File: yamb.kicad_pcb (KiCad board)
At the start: 2 copper layers, 67.7 x 96.7 mm, 18 parts, among them J1 Barrel_Jack, J2 I2C, J3 HEADER, J4 HEADER_2.54, J5 Remote_Reset, J6 Power_Switch, P1 USB_C_Plug_USB2.0, SW1 RESET, U1 TPS3808DBV, U2 MCSBC, U3 SVR, U4 RAK4630, U5 BME280

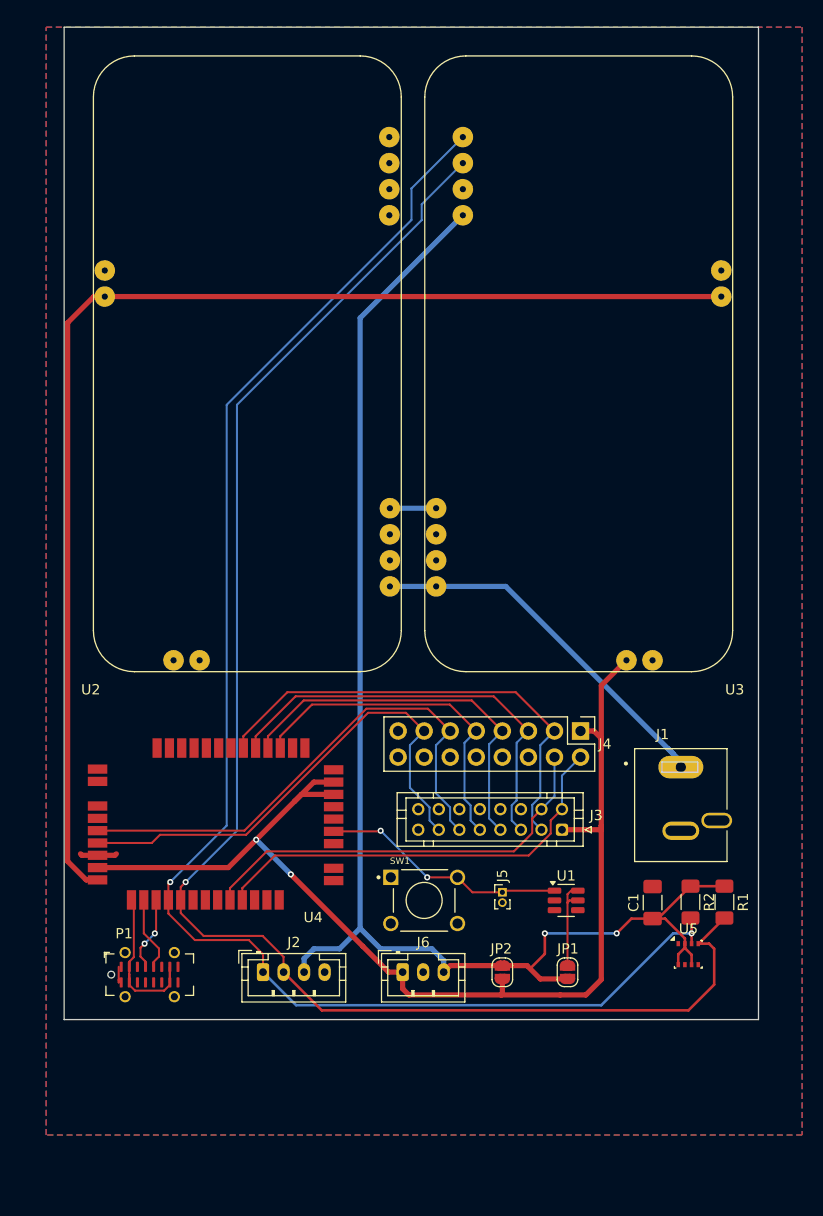
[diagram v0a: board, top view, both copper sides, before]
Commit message: changed connectors to shroued 0.1" and cleaned some board DRC errors
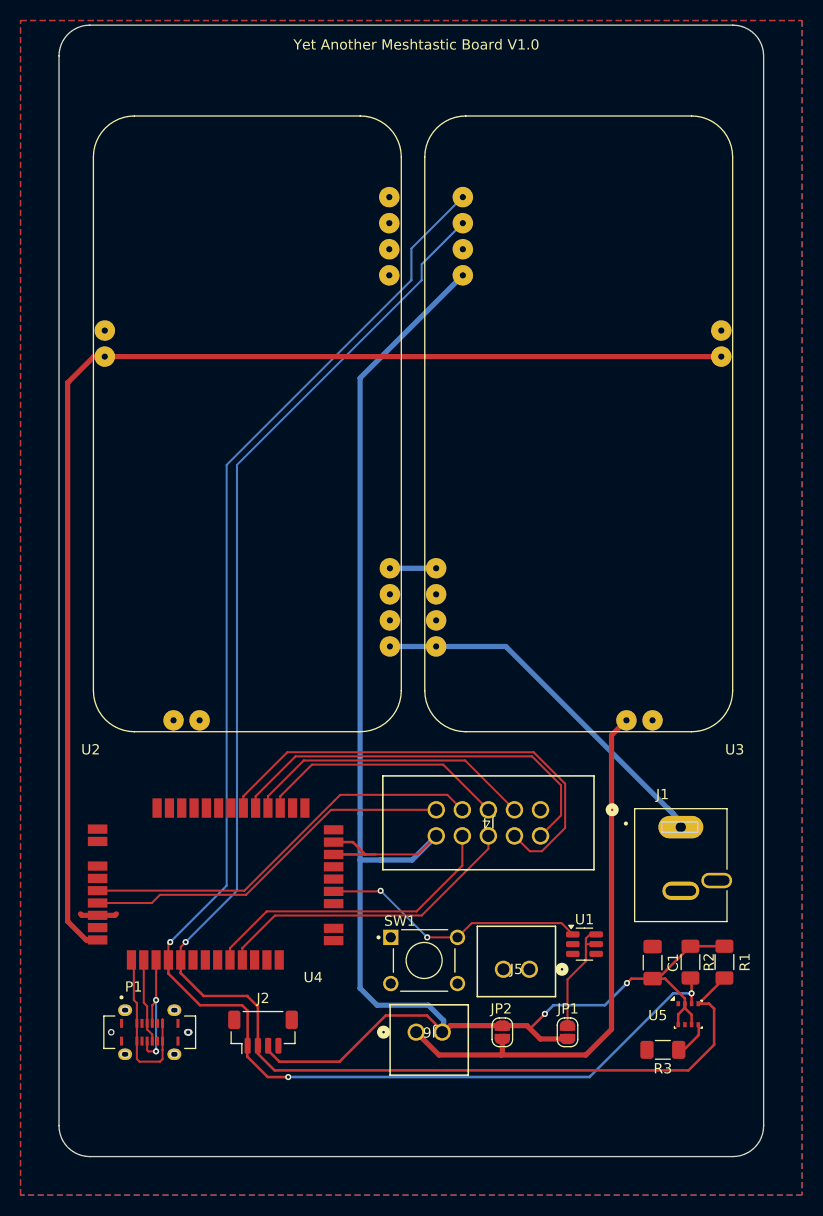
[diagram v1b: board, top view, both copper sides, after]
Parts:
- removed J3: HEADER, Connector_JST:JST_PHD_B16B-PHDSS_2x08_P2.00mm_Vertical
- added R3: 10K, Resistor_SMD:R_1206_3216Metric_Pad1.30x1.75mm_HandSolder, F.Cu at (165.5, 112.3)
- C1: value BMECAP -> 100n
- J2: footprint Connector_JST:JST_PH_B4B-PH-K_1x04_P2.00mm_Vertical -> Connector_JST:JST_SH_BM04B-SRSS-TB_1x04-1MP_P1.00mm_Vertical
- J4: footprint Connector_PinHeader_2.54mm:PinHeader_2x08_P2.54mm_Vertical -> Andy_Footprints:CONN_7024610xx_MOL
- J5: footprint Connector_PinHeader_1.00mm:PinHeader_1x02_P1.00mm_Vertical -> Andy_Footprints:CONN_SDA-70543-xxxx_02_MOL
- J6: footprint Connector_JST:JST_PH_B3B-PH-K_1x03_P2.00mm_Vertical -> Andy_Footprints:CONN_SDA-70543-xxxx_02_MOL
- P1: footprint Connector_USB:USB_C_Receptacle_G-Switch_GT-USB-7051x -> Andy_Footprints:SAMESKY_UJ20-C-V-G-SMT-P16-TR
- R1, R2: value R -> 4.7K
- moved J4 8.61 mm to (153.6, 89.0), turned to 180 degrees
- moved J5 7.95 mm to (152.5, 104.5)
- moved J6 6.00 mm to (141.5, 110.6), turned to 180 degrees
- moved U4 5.85 mm to (121.9, 97.3)
- moved U3 5.85 mm to (141.3, 20.4)
- moved C1 5.85 mm to (164.5, 103.8)
- moved J1 5.85 mm to (167.2, 94.3)
- moved J2 5.85 mm to (126.5, 110.6)
- moved JP1 5.85 mm to (156.2, 110.6)
- moved JP2 5.85 mm to (149.9, 110.6)
- moved R1 5.85 mm to (171.5, 103.8)
- moved R2 5.85 mm to (168.2, 103.8)
- moved SW1 5.85 mm to (142.2, 103.6)
- moved U2 5.85 mm to (141.0, 82.3)
- moved U5 5.85 mm to (168.0, 108.9)
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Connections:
- net WATCHDOGVDD renamed /WATCHDOG
- J4 pad 1: 3V3 -> GND
- J4 pad 10: unconnected-(J4-Pin_10-Pad10) -> 3V3
- J4 pad 2: UART_TX -> SW2
- J4 pad 3: LED2 -> SW1
- J4 pad 4: UAART_RX -> AIN3
- J4 pad 5: LED1 -> AIN2
- J4 pad 6: unconnected-(J4-Pin_6-Pad6) -> LED1
- J4 pad 7: SW2 -> LED2
- J4 pad 8: unconnected-(J4-Pin_8-Pad8) -> UART_TX
- J4 pad 9: SW1 -> UAART_RX
- J6 pad 2: unconnected-(J6-Pin_2-Pad2) -> 3V3
- P1 pad A6: USB+ -> USB-
- P1 pad A7: USB- -> USB+
- P1 pad B6: unconnected-(P1-D+-PadB6) -> USB-
- P1 pad B7: unconnected-(P1-D--PadB7) -> USB+
- U2 pad 3: unconnected-(U2-GND-Pad3) -> GND
- U2 pad 4: unconnected-(U2-VLOAD_IN-Pad4) -> 3V3
- U4 pad 43: 3V3 -> unconnected-(U4-VDD_NRF-Pad43)
- U5 pad 5: GND -> /BMEADDRESS
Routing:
- net +3.3V: track 120.3 -> 53.3 mm, vias 2 -> 0
- net 3V3: track 137.6 -> 170.7 mm
- net AIN2: track 49.2 -> 36.8 mm
- net UART_TX: track 42.1 -> 30.4 mm
- net AIN3: track 51.3 -> 40.0 mm
- net UAART_RX: track 41.1 -> 30.0 mm
- net SW1: track 33.3 -> 24.5 mm
- net SW2: track 37.3 -> 28.6 mm
- net USB+: track 7.35 -> 13.1 mm
- net /BMEADDRESS: track 0.00 -> 3.10 mm
- net SDA: track 148.7 -> 151.1 mm, vias 2 -> 3
- net /WATCHDOG: track 9.20 -> 11.4 mm
- net RESET: track 24.2 -> 26.4 mm
- net LED1: track 41.4 -> 39.4 mm
- net GND: track 5.43 -> 3.62 mm
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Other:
- board size 67.7 x 96.7 mm -> 68.7 x 110.2 mm
- board text added: "Yet Another Meshtastic Board V1.0"
